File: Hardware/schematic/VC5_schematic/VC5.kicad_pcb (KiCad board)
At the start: 2 copper layers, 167.9 x 73.3 mm, 59 parts, among them J1 Debug_output, Q1 BC337, U1 1.3in SH1106 OLED, U2 1.3in SH1106 OLED, U3 1.3in SH1106 OLED, U4 1.3in SH1106 OLED, U5 1.3in SH1106 OLED, U6 MCP23017

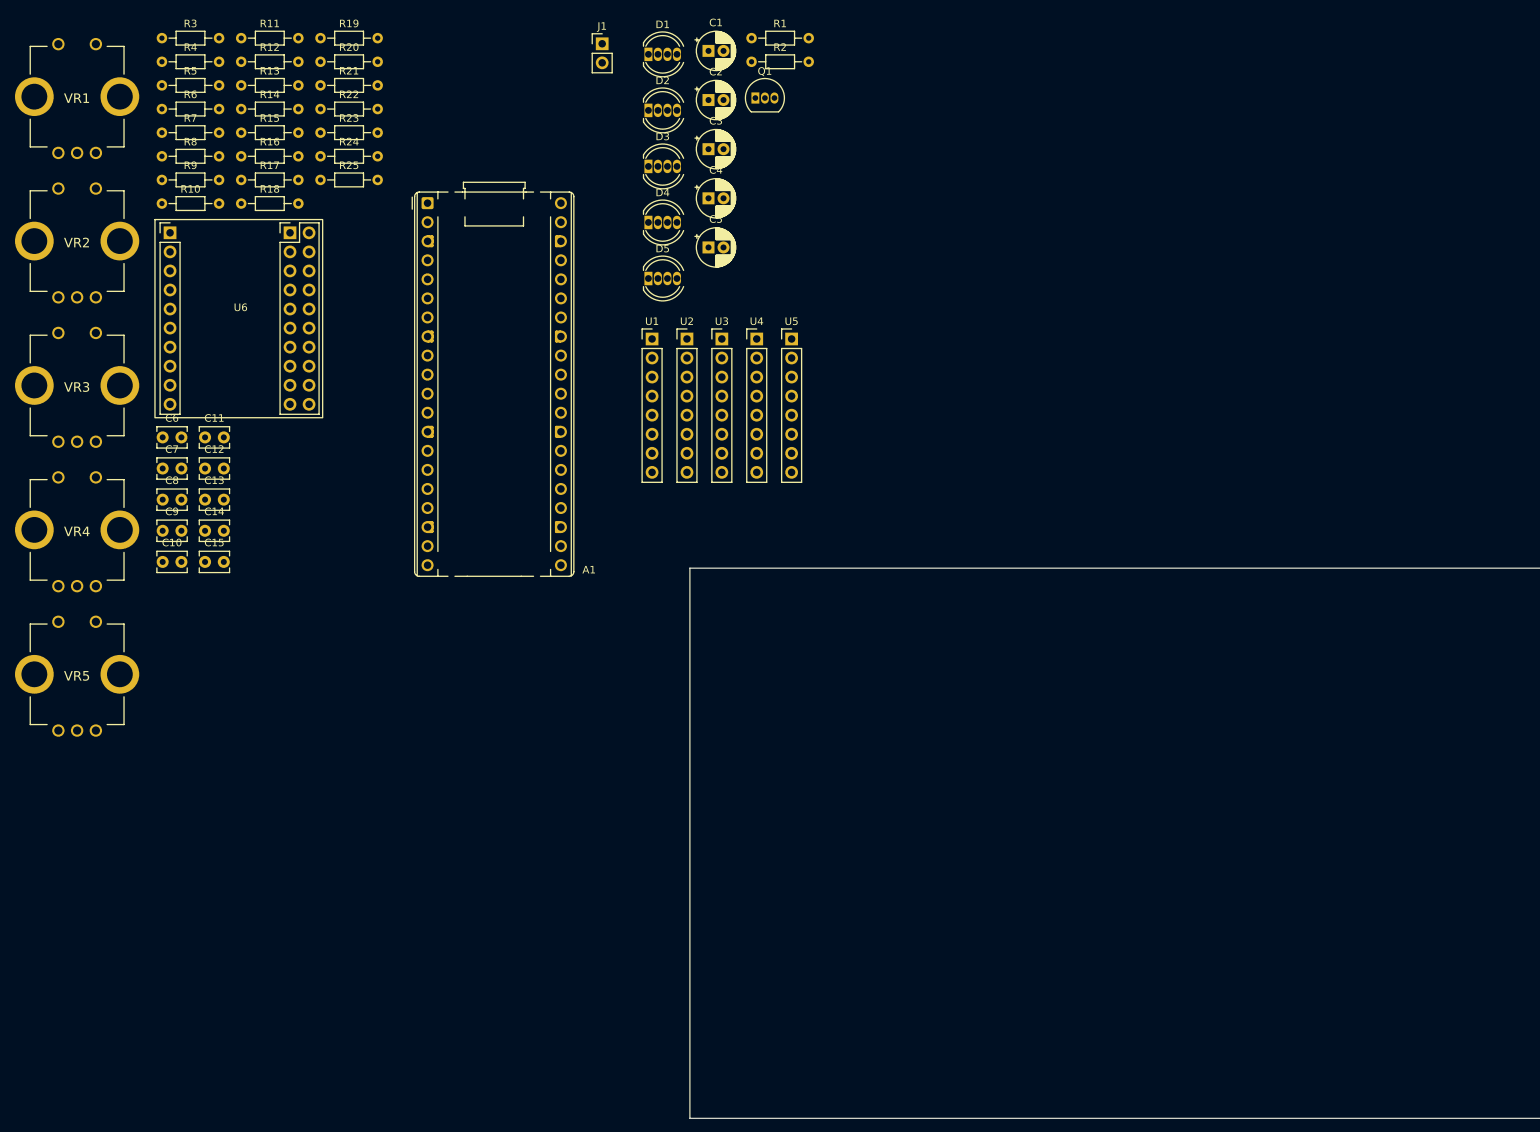
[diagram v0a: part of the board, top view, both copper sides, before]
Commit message: updated footprints and corresponding 3D models
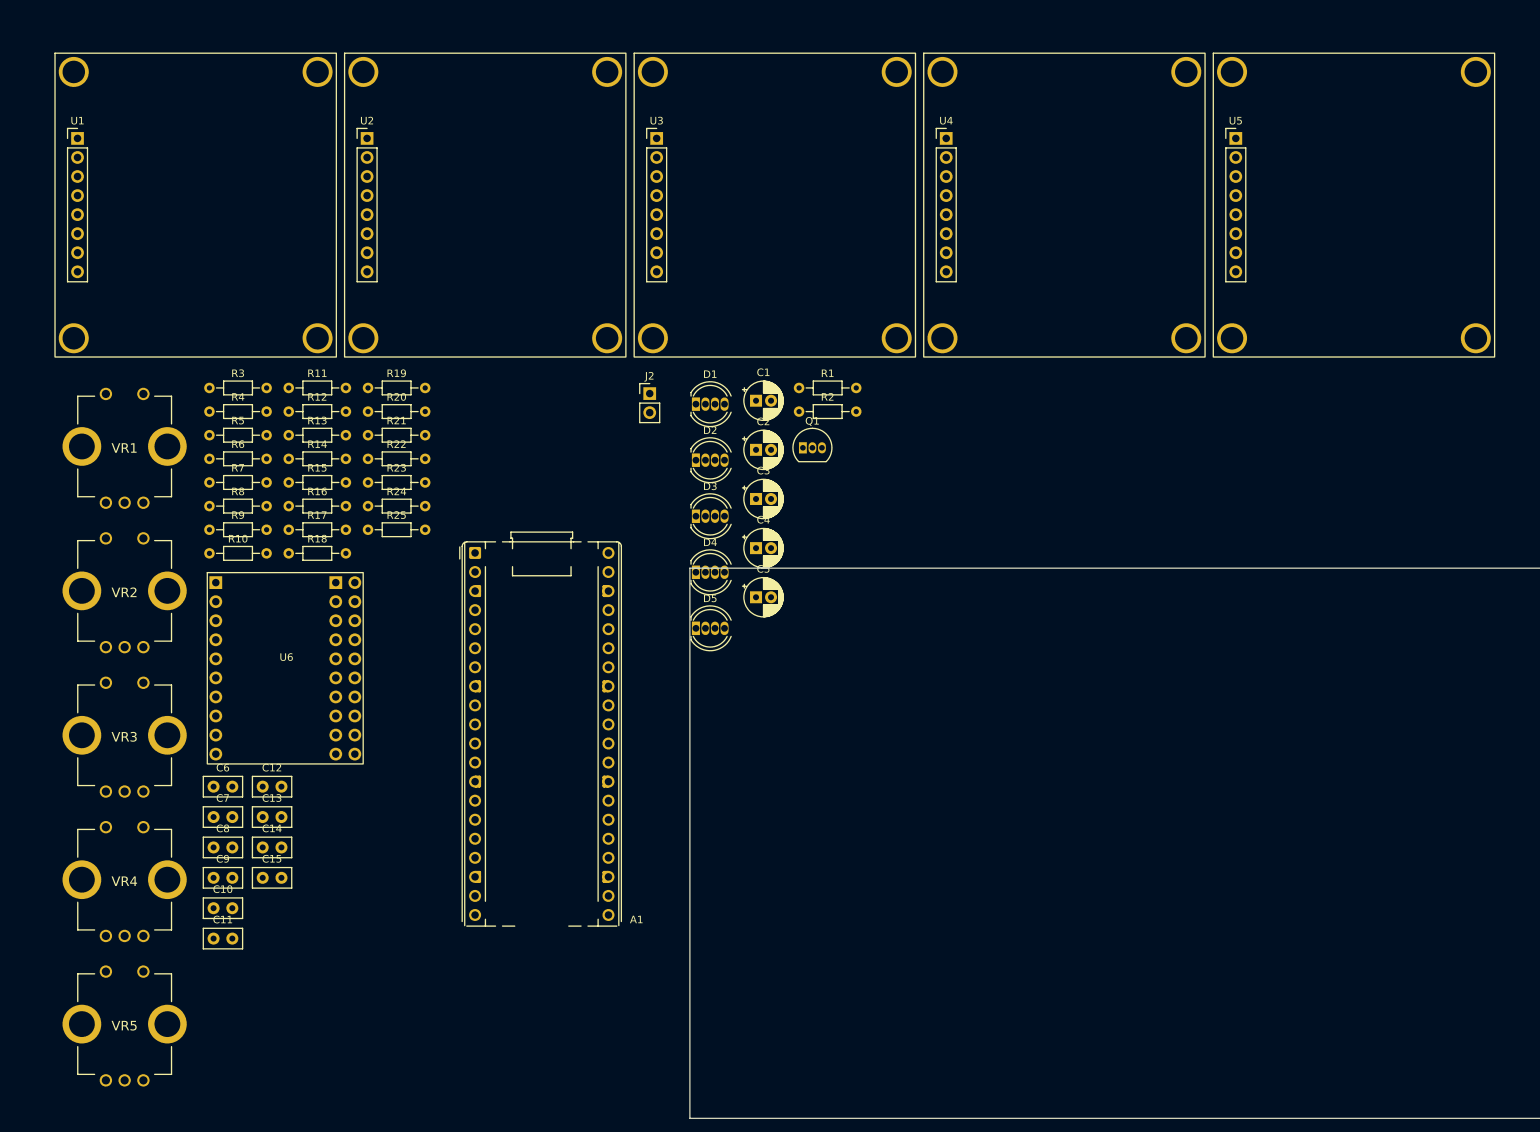
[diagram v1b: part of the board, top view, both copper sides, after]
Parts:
- removed J1: Debug_output, Connector_PinHeader_2.54mm:PinHeader_1x02_P2.54mm_Vertical
- added J2: Debug_output, Connector_PinHeader_2.54mm:PinHeader_1x02_P2.54mm_Vertical, F.Cu at (99.8, 63.2)
- A1: footprint Module:RaspberryPi_Pico_Common_THT -> VC5_footprint_library:RaspberryPi_Pico_Common_THT_custom
- C10, C11, C12, C13, C14, C15, C6, C7, C8, C9: footprint Capacitor_THT:C_Disc_D3.8mm_W2.6mm_P2.50mm -> Capacitor_THT:C_Disc_D5.0mm_W2.5mm_P2.50mm
- U1, U2, U3, U4, U5: footprint Connector_PinHeader_2.54mm:PinHeader_1x08_P2.54mm_Vertical -> VC5_footprint_library:PinHeader_1x08_P2.54mm_Vertical_Display
- VR1, VR2, VR3, VR4, VR5: footprint VC5_footprint_library:PEC11R_4220F_S0024 -> VC5_footprint_library:PEC11R4220FS0024
- moved U1 81.1 mm to (23.6, 29.2)
- moved C11 66.8 mm to (41.7, 135.8)
- moved U5 65.0 mm to (178.0, 29.2)
- moved U2 50.3 mm to (62.2, 29.2)
- moved R15 47.1 mm to (51.7, 75.0)
- moved R23 47.1 mm to (62.3, 75.0)
- moved R7 47.1 mm to (41.2, 75.0)
- moved D2 47.1 mm to (106.0, 72.1)
- moved R12 47.1 mm to (51.7, 65.6)
- moved R17 47.1 mm to (51.7, 81.3)
- moved R20 47.1 mm to (62.3, 65.6)
- moved R25 47.1 mm to (62.3, 81.3)
- moved R4 47.1 mm to (41.2, 65.6)
- moved R9 47.1 mm to (41.2, 81.3)
- moved VR1 47.1 mm to (27.4, 63.2)
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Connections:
- R10 pad 1: GND -> +3.3V
- R11 pad 1: GND -> +3.3V
- R14 pad 1: GND -> +3.3V
- R15 pad 1: GND -> +3.3V
- R18 pad 1: GND -> +3.3V
- R19 pad 1: GND -> +3.3V
- R22 pad 1: GND -> +3.3V
- R23 pad 1: GND -> +3.3V
- R3 pad 1: GND -> +3.3V
- R4 pad 1: GND -> +3.3V

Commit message: added pcb parameters, positioned LEDs
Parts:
- A1, U6: moved to B.Cu
- moved VR5 223.5 mm to (247.6, 102.3)
- moved U6 180.4 mm to (229.6, 79.3), turned to -90 degrees
- moved VR4 177.3 mm to (203.7, 102.3)
- moved VR3 137.3 mm to (164.6, 102.3)
- moved D5 133.8 mm to (238.1, 115.6), turned to -90 degrees
- moved VR2 97.8 mm to (123.1, 102.3)
- moved D4 92.7 mm to (194.2, 115.6), turned to -90 degrees
- moved U5 92.5 mm to (241.2, 96.6), turned to 90 degrees
- moved U4 90.5 mm to (199.8, 96.6), turned to 90 degrees
- moved U3 88.6 mm to (158.2, 96.6), turned to 90 degrees
- moved U2 86.8 mm to (116.8, 96.6), turned to 90 degrees
- moved U1 85.0 mm to (75.2, 96.6), turned to 90 degrees
- moved A1 72.6 mm to (149.0, 89.2), turned to 90 degrees
- moved VR1 66.9 mm to (81.6, 102.3)
- moved J2 66.2 mm to (160.7, 89.2), turned to -90 degrees
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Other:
- board size 167.9 x 73.3 mm -> 212.4 x 78.8 mm

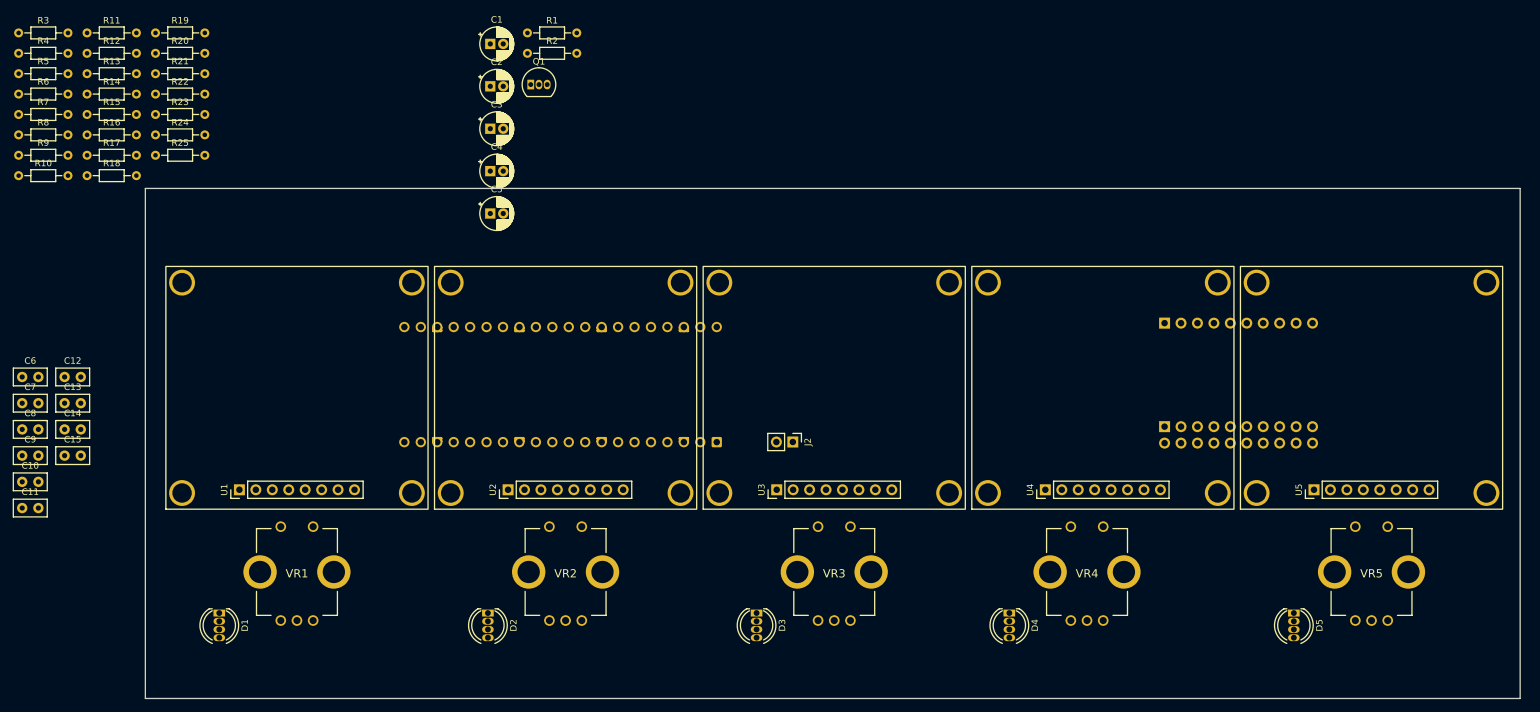
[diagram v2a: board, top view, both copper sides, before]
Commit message: trace routing completed
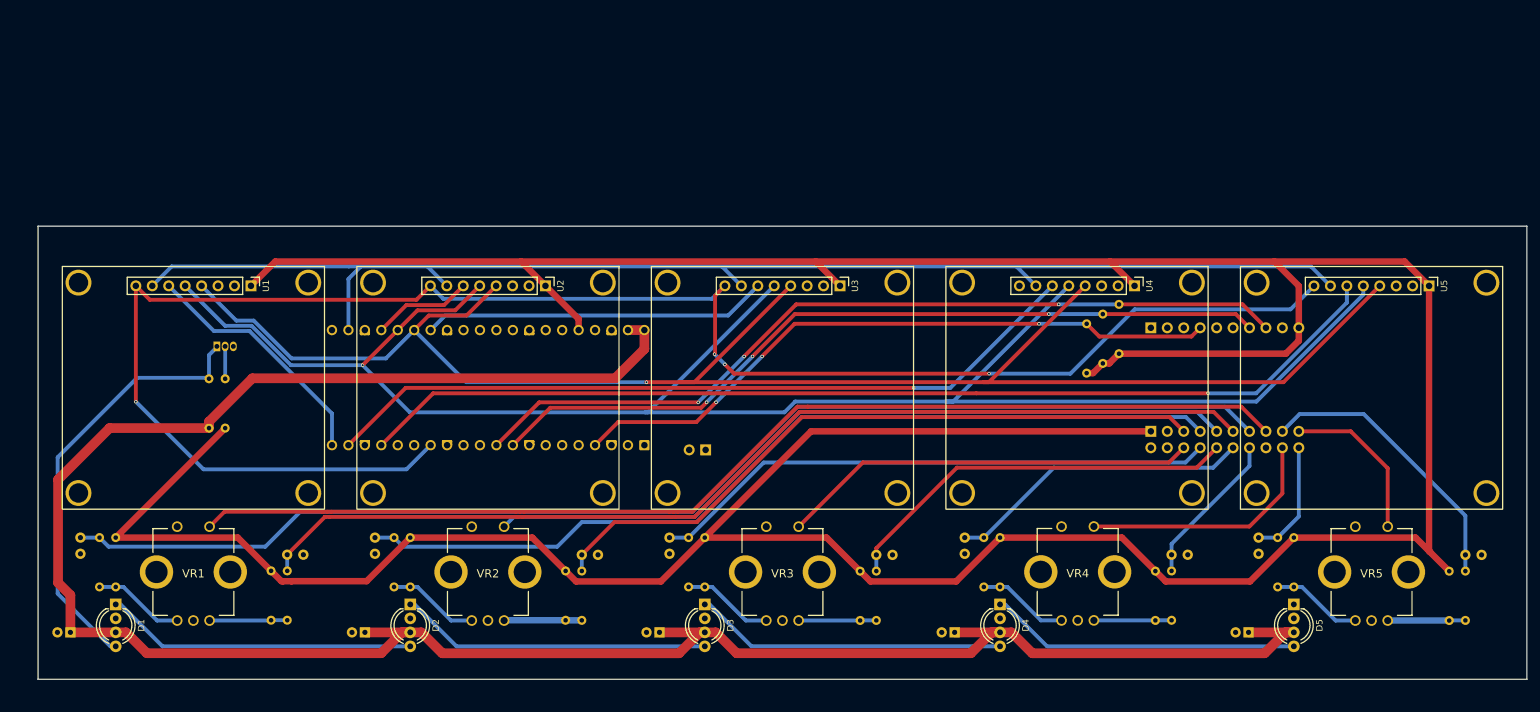
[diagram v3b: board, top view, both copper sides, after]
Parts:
- C1, C10, C11, C12, C13, C14, C15, C2, C3, C4, C5, C6, C7, C8, C9, J2, Q1, R1, R10, R11, R12, R13, R14, R15, R16, R17, R18, R19, R2, R20, R21, R22, R23, R24, R25, R3, R4, R5, R6, R7, R8, R9: moved to B.Cu
- D1, D2, D3, D4, D5: footprint LED_THT:LED_D5.0mm-4_RGB -> LED_THT:LED_D5.0mm-4_RGB_Wide_Pins
- moved C15 216.9 mm to (264.6, 106.7)
- moved R25 214.7 mm to (264.6, 116.8), turned to 90 degrees
- moved R22 213.0 mm to (262.1, 109.2), turned to -90 degrees
- moved R23 187.6 mm to (238.1, 104.0), turned to -90 degrees
- moved R24 186.9 mm to (235.6, 111.6), turned to 90 degrees
- moved C14 185.2 mm to (232.7, 104.0), turned to -90 degrees
- moved R21 178.2 mm to (219.2, 116.8), turned to 90 degrees
- moved R18 176.0 mm to (216.8, 109.2), turned to -90 degrees
- moved C13 172.6 mm to (219.2, 106.6)
- moved R8 172.0 mm to (211.1, 68.0), turned to -90 degrees
- moved R7 170.3 mm to (208.6, 69.5), turned to -90 degrees
- moved R9 168.4 mm to (206.1, 78.6), turned to 90 degrees
- moved R20 152.2 mm to (190.2, 111.6), turned to 90 degrees
- moved R19 152.0 mm to (192.8, 104.0), turned to -90 degrees
- moved R17 141.5 mm to (173.6, 116.8), turned to 90 degrees
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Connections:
- A1 pad 16: /displays/CS0 -> unconnected-(A1-GPIO12-Pad16)
- A1 pad 17: /displays/CS1 -> /displays/CS4
- A1 pad 19: /displays/CS2 -> /displays/CS3
- A1 pad 20: /displays/CS4 -> /displays/CS0
- A1 pad 21: /displays/D/C -> /LEDs/LED
- A1 pad 22: /displays/CS3 -> /displays/D/C
- A1 pad 24: /displays/CLK -> /displays/CS1
- A1 pad 25: /displays/DIN -> /displays/CLK
- A1 pad 26: /LEDs/LED -> /displays/DIN
- A1 pad 27: unconnected-(A1-GPIO21-Pad27) -> /displays/CS2
- C10 pad 1: Net-(U6-GPB7) -> Net-(U6-GPA1)
- C11 pad 1: Net-(U6-GPA7) -> Net-(U6-GPA2)
- C12 pad 1: Net-(U6-GPB2) -> Net-(U6-GPA3)
- C13 pad 1: Net-(U6-GPB1) -> Net-(U6-GPA4)
- C14 pad 1: Net-(U6-GPB4) -> Net-(U6-GPA7)
- C15 pad 1: Net-(U6-GPB3) -> Net-(U6-GPB6)
- C6 pad 1: Net-(U6-GPA1) -> Net-(U6-GPB4)
- C7 pad 1: Net-(U6-GPA0) -> Net-(U6-GPB3)
- C8 pad 1: Net-(U6-GPA4) -> Net-(U6-GPB1)
- C9 pad 1: Net-(U6-GPA5) -> Net-(U6-GPB0)
- R12 pad 2: Net-(U6-GPA4) -> Net-(U6-GPB1)
- R13 pad 2: Net-(U6-GPA5) -> Net-(U6-GPB0)
- R16 pad 2: Net-(U6-GPB7) -> Net-(U6-GPA1)
- R17 pad 2: Net-(U6-GPA7) -> Net-(U6-GPA2)
- R20 pad 2: Net-(U6-GPB2) -> Net-(U6-GPA3)
- R21 pad 2: Net-(U6-GPB1) -> Net-(U6-GPA4)
- R24 pad 2: Net-(U6-GPB4) -> Net-(U6-GPA7)
- R25 pad 2: Net-(U6-GPB3) -> Net-(U6-GPB6)
- R5 pad 2: Net-(U6-GPA1) -> Net-(U6-GPB4)
- R6 pad 2: Net-(U6-GPA0) -> Net-(U6-GPB3)
- U6 pad 22: Net-(U6-GPA5) -> unconnected-(U6-GPA5-Pad22)
- U6 pad 25: unconnected-(U6-GPB0-Pad25) -> Net-(U6-GPB0)
- VR1 pad 2: Net-(U6-GPA2) -> Net-(U6-GPB5)
- VR2 pad 2: Net-(U6-GPA3) -> Net-(U6-GPB2)
- VR3 pad 2: Net-(U6-GPA6) -> Net-(U6-GPA0)
- VR4 pad 2: Net-(U6-GPB6) -> Net-(U6-GPA6)
- VR5 pad 2: Net-(U6-GPB5) -> Net-(U6-GPB7)
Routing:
- net +3.3V: track 0.00 -> 630.1 mm
- net +5V: track 0.00 -> 357.1 mm
- net /displays/CLK: track 0.00 -> 276.5 mm, vias 0 -> 1
- net /displays/DISP_RESET: track 0.00 -> 274.4 mm, vias 0 -> 4
- net /displays/DIN: track 0.00 -> 258.6 mm, vias 0 -> 1
- net /displays/D/C: track 0.00 -> 207.9 mm
- net Net-(U6-GPB4): track 0.00 -> 191.7 mm
- net Net-(U6-GPB5): track 0.00 -> 172.4 mm
- net /displays/CS4: track 0.00 -> 160.9 mm, vias 0 -> 1
- net Net-(U6-GPB3): track 0.00 -> 159.0 mm
- net Net-(U6-GPB1): track 0.00 -> 137.3 mm
- net /rotaries/I2C_SCL: track 0.00 -> 129.4 mm, vias 0 -> 3
- net /rotaries/I2C_SDA: track 0.00 -> 123.1 mm, vias 0 -> 3
- net /displays/CS3: track 0.00 -> 118.9 mm, vias 0 -> 1
- net Net-(U6-GPB2): track 0.00 -> 118.7 mm
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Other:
- board size 212.4 x 78.8 mm -> 230 x 70 mm

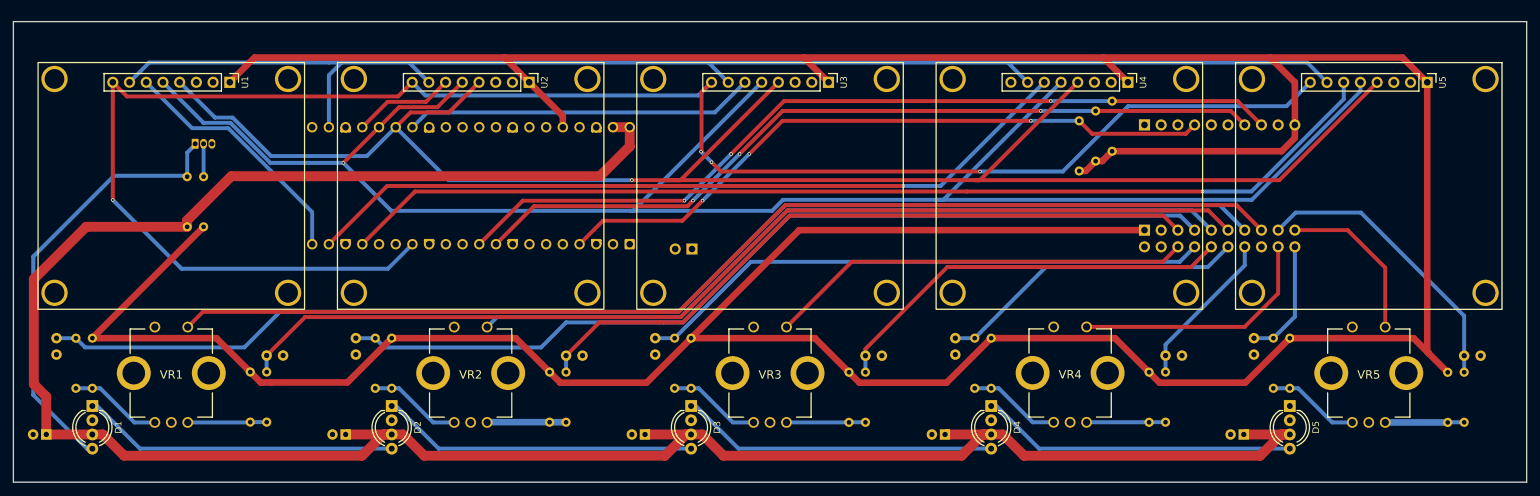
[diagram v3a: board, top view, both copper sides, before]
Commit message: added final trace adjustments and mounting holes
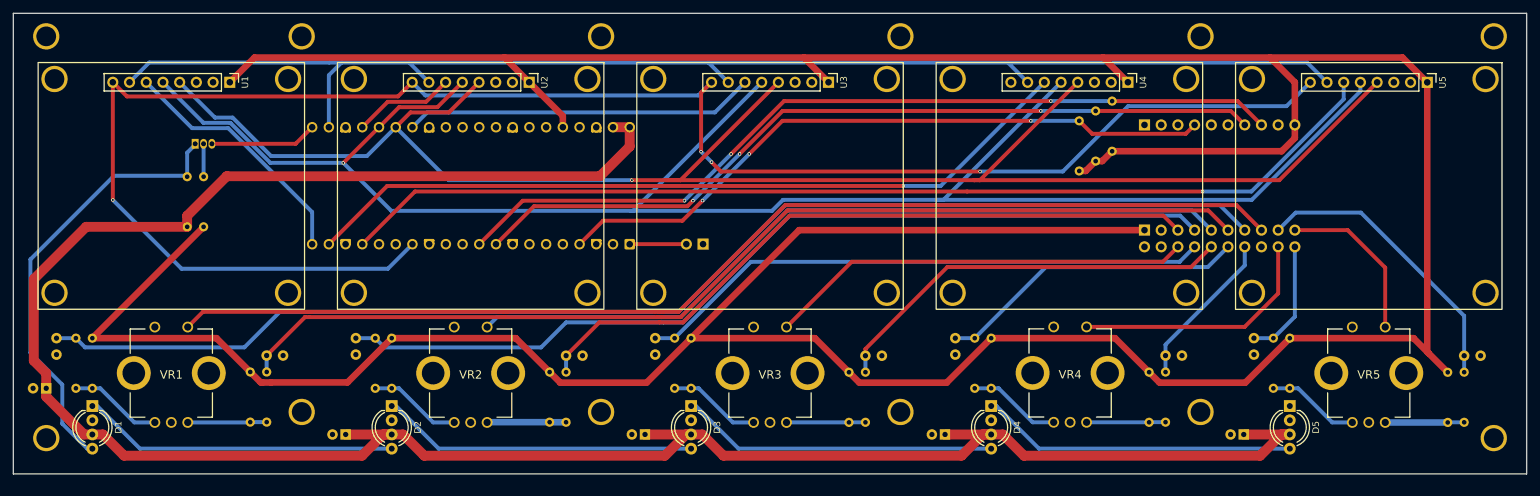
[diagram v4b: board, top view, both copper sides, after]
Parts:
- added ?: , , F.Cu at (49.1, 119.2)
- added ?: , , F.Cu at (224.6, 58.1)
- added ?: , , F.Cu at (88.0, 58.1)
- added ?: , , F.Cu at (269.1, 119.2)
- added ?: , , F.Cu at (179.0, 58.1)
- added ?: , , F.Cu at (269.1, 58.1)
- added ?: , , F.Cu at (133.5, 58.1)
- added ?: , , F.Cu at (88.0, 115.2)
- added ?: , , F.Cu at (49.1, 58.1)
- added ?: , , F.Cu at (225.0, 115.2)
- added ?: , , F.Cu at (133.3, 115.2)
- added ?: , , F.Cu at (179.2, 115.2)
- moved C1 7.02 mm to (49.1, 111.6)
- moved J2 1.84 mm to (149.0, 89.7)
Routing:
- net /LEDs/LED: track 0.00 -> 16.3 mm
- net Net-(A1-GPIO0): track 0.00 -> 8.61 mm
- net +5V: track 357.1 -> 354.1 mm

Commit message: first final version
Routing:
- net /displays/DISP_RESET: track 274.4 -> 293.6 mm, vias 4 -> 5
- net /displays/CLK: track 276.5 -> 278.7 mm
- added copper zone on B.Cu, net GND
- added copper zone on F.Cu, net GND
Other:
- board text added: "BOT"
- board text added: "TOP"
